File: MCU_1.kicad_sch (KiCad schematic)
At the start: 4 parts, among them U2 LPC55S28JBD100, Y1 24MHz

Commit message: Reset devresi eklenecek.
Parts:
- added C? (x2): 18pF, Resistor_SMD:R_0603_1608Metric, symbol Device:C
- added R?: R, symbol Device:R
- added SW?: SW_SPST, symbol Switch:SW_SPST
- added Y?: 24MHz, Crystal:Crystal_SMD_HC49-SD, symbol Device:Crystal
- U2: footprint erkan-hw-lib:HLQFP100 -> HLQFP100
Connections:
- net GND: now also C?.2, C?.2
- net MCU_XTAL32M_N: now also C?.1, Y?.1
- net MCU_XTAL32M_P: now also C?.1, Y?.2
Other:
- note added: "JTAG"
- note added: "MCU RESET"
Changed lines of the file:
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@@
   (junction (at 247.65 33.655) (diameter 0) (color 0 0 0 0)
   )
+  (junction (at 180.975 34.29) (diameter 0) (color 0 0 0 0)
+  )
   (junction (at 247.65 51.435) (diameter 0) (color 0 0 0 0)
   )
+  (junction (at 180.975 52.07) (diameter 0) (color 0 0 0 0)
+  )
   (wire (pts (xy 279.4 23.495) (xy 279.4 57.785))
     (stroke (width 0.5) (type solid) (color 57 87 255 1))
   )
+  (wire (pts (xy 191.135 34.29) (xy 180.975 34.29))
+    (stroke (width 0) (type default) (color 0 0 0 0))
+  )
   (wire (pts (xy 241.935 33.655) (xy 247.65 33.655))
     (stroke (width 0) (type default) (color 0 0 0 0))
@@
     (stroke (width 0) (type default) (color 0 0 0 0))
   )
+  (wire (pts (xy 223.52 100.965) (xy 280.035 100.965))
+    (stroke (width 0.5) (type solid) (color 57 87 255 1))
+  )
+  (wire (pts (xy 175.26 34.29) (xy 180.975 34.29))
+    (stroke (width 0) (type default) (color 0 0 0 0))
+  )
+  (wire (pts (xy 156.21 24.13) (xy 156.21 58.42))
+    (stroke (width 0.5) (type default) (color 57 87 255 1))
+  )
+  (wire (pts (xy 280.035 66.675) (xy 280.035 100.965))
+    (stroke (width 0.5) (type solid) (color 57 87 255 1))
+  )
   (wire (pts (xy 222.885 57.785) (xy 279.4 57.785))
     (stroke (width 0.5) (type solid) (color 57 87 255 1))
   )
+  (wire (pts (xy 191.135 52.07) (xy 180.975 52.07))
+    (stroke (width 0) (type default) (color 0 0 0 0))
+  )
+  (wire (pts (xy 223.52 66.675) (xy 280.035 66.675))
+    (stroke (width 0.5) (type default) (color 57 87 255 1))
+  )
   (wire (pts (xy 222.885 23.495) (xy 279.4 23.495))
     (stroke (width 0.5) (type default) (color 57 87 255 1))
   )
+  (wire (pts (xy 180.975 34.29) (xy 180.975 38.735))
+    (stroke (width 0) (type default) (color 0 0 0 0))
+  )
+  (wire (pts (xy 180.975 52.07) (xy 180.975 46.355))
+    (stroke (width 0) (type default) (color 0 0 0 0))
+  )
   (wire (pts (xy 247.65 33.655) (xy 247.65 38.1))
     (stroke (width 0) (type default) (color 0 0 0 0))
   )
+  (wire (pts (xy 175.26 52.07) (xy 180.975 52.07))
+    (stroke (width 0) (type default) (color 0 0 0 0))
+  )
+  (wire (pts (xy 223.52 66.675) (xy 223.52 100.965))
+    (stroke (width 0.5) (type default) (color 57 87 255 1))
+  )
+  (wire (pts (xy 156.21 24.13) (xy 212.725 24.13))
+    (stroke (width 0.5) (type default) (color 57 87 255 1))
+  )
+  (wire (pts (xy 212.725 24.13) (xy 212.725 58.42))
+    (stroke (width 0.5) (type solid) (color 57 87 255 1))
+  )
+  (wire (pts (xy 156.21 58.42) (xy 212.725 58.42))
+    (stroke (width 0.5) (type solid) (color 57 87 255 1))
+  )
   (wire (pts (xy 247.65 51.435) (xy 247.65 45.72))
     (stroke (width 0) (type default) (color 0 0 0 0))
@@
   (wire (pts (xy 257.81 33.655) (xy 247.65 33.655))
     (stroke (width 0) (type default) (color 0 0 0 0))
+  )
+  (text "JTAG" (at 155.575 23.495 0)
+    (effects (font (size 2.5 2.5) (thickness 0.5) bold) (justify left bottom))
   )
   (text "CRYSTAL-HSE" (at 222.25 22.86 0)
     (effects (font (size 2.5 2.5) (thickness 0.5) bold) (justify left bottom))
   )
+  (text "MCU RESET" (at 222.885 66.04 0)
+    (effects (font (size 2.5 2.5) (thickness 0.5) bold) (justify left bottom))
+  )
+  (label "MCU_XTAL32M_P" (at 175.26 34.29 180)
+    (effects (font (size 1.27 1.27)) (justify right bottom))
+  )
   (label "MCU_XTAL32M_P" (at 241.935 33.655 180)
     (effects (font (size 1.27 1.27)) (justify right bottom))
   )
-  (label "MCU_XTAL32M_P" (at 38.1 36.195 180)
-    (effects (font (size 1.27 1.27)) (justify right bottom))
-  )
-  (label "MCU_XTAL32M_N" (at 38.1 38.735 180)
+  (label "MCU_XTAL32M_P" (at 33.655 40.005 180)
+    (effects (font (size 1.27 1.27)) (justify right bottom))
+  )
+  (label "MCU_XTAL32M_N" (at 33.655 42.545 180)
     (effects (font (size 1.27 1.27)) (justify right bottom))
   )
   (label "MCU_XTAL32M_N" (at 241.935 51.435 180)
     (effects (font (size 1.27 1.27)) (justify right bottom))
+  )
+  (label "MCU_XTAL32M_N" (at 175.26 52.07 180)
+    (effects (font (size 1.27 1.27)) (justify right bottom))
+  )
+  (symbol (lib_id "Device:C") (at 194.945 52.07 90) (unit 1)
+    (in_bom yes) (on_board yes) (fields_autoplaced)
+    (property "Reference" "C?" (id 0) (at 194.945 45.085 90))
+    (property "Value" "18pF" (id 1) (at 194.945 47.625 90))
+    (property "Footprint" "Resistor_SMD:R_0603_1608Metric" (id 2) (at 198.755 51.1048 0)
+      (effects (font (size 1.27 1.27)) hide)
+    )
+    (property "Datasheet" "~" (id 3) (at 194.945 52.07 0)
+      (effects (font (size 1.27 1.27)) hide)
+    )
+    (pin "1")
+    (pin "2")
   )
   (symbol (lib_id "Device:C") (at 261.62 51.435 90) (unit 1)
@@
     (pin "1")
   )
-  (symbol (lib_id "erkan-hw:LPC55S28JBD100") (at 38.1 26.035 0) (unit 1)
-    (in_bom yes) (on_board yes) (fields_autoplaced)
-    (property "Reference" "U2" (id 0) (at 83.82 15.24 0)
+  (symbol (lib_id "Switch:SW_SPST") (at 243.84 84.455 0) (unit 1)
+    (in_bom yes) (on_board yes) (fields_autoplaced)
+    (property "Reference" "SW?" (id 0) (at 243.84 77.47 0))
+    (property "Value" "SW_SPST" (id 1) (at 243.84 80.01 0))
+    (property "Footprint" "" (id 2) (at 243.84 84.455 0)
+      (effects (font (size 1.27 1.27)) hide)
+    )
+    (property "Datasheet" "~" (id 3) (at 243.84 84.455 0)
+      (effects (font (size 1.27 1.27)) hide)
+    )
+    (pin "1")
+    (pin "2")
+  )
+  (symbol (lib_id "erkan-hw:LPC55S28JBD100") (at 17.145 29.845 0) (unit 1)
+    (in_bom yes) (on_board yes)
+    (property "Reference" "U2" (id 0) (at 79.375 18.415 0)
       (effects (font (size 1.524 1.524)))
     )
-    (property "Value" "LPC55S28JBD100" (id 1) (at 83.82 19.05 0)
+    (property "Value" "LPC55S28JBD100" (id 1) (at 79.375 22.225 0)
       (effects (font (size 1.524 1.524)))
     )
-    (property "Footprint" "erkan-hw-lib:HLQFP100" (id 2) (at 83.82 19.939 0)
+    (property "Footprint" "HLQFP100" (id 2) (at 37.465 14.859 0)
       (effects (font (size 1.524 1.524)) hide)
     )
-    (property "Datasheet" "" (id 3) (at 38.1 26.035 0)
+    (property "Datasheet" "" (id 3) (at 17.145 29.845 0)
       (effects (font (size 1.524 1.524)))
     )
@@
     (pin "42")
     (pin "43")
-    (pin "45")
-    (pin "48")
-    (pin "49")
     (pin "5")
-    (pin "50")
-    (pin "51")
     (pin "52")
     (pin "53")
@@
     (pin "33")
     (pin "37")
-    (pin "39")
     (pin "44")
-    (pin "46")
-    (pin "47")
     (pin "63")
     (pin "69")
@@
     (pin "95")
     (pin "99")
+    (pin "39")
+    (pin "45")
+    (pin "46")
+    (pin "47")
+    (pin "48")
+    (pin "49")
+    (pin "50")
+    (pin "51")
   )
   (symbol (lib_id "power:GND") (at 265.43 33.655 90) (unit 1)
@@
     (pin "2")
   )
+  (symbol (lib_id "power:GND") (at 198.755 34.29 90) (unit 1)
+    (in_bom yes) (on_board yes) (fields_autoplaced)
+    (property "Reference" "#PWR?" (id 0) (at 205.105 34.29 0)
+      (effects (font (size 1.27 1.27)) hide)
+    )
+    (property "Value" "GND" (id 1) (at 202.565 34.2899 90)
+      (effects (font (size 1.27 1.27)) (justify right))
+    )
+    (property "Footprint" "" (id 2) (at 198.755 34.29 0)
+      (effects (font (size 1.27 1.27)) hide)
+    )
+    (property "Datasheet" "" (id 3) (at 198.755 34.29 0)
+      (effects (font (size 1.27 1.27)) hide)
+    )
+    (pin "1")
+  )
+  (symbol (lib_id "Device:Crystal") (at 180.975 42.545 90) (unit 1)
+    (in_bom yes) (on_board yes) (fields_autoplaced)
+    (property "Reference" "Y?" (id 0) (at 184.785 41.2749 90)
+      (effects (font (size 1.27 1.27)) (justify right))
+    )
+    (property "Value" "24MHz" (id 1) (at 184.785 43.8149 90)
+      (effects (font (size 1.27 1.27)) (justify right))
+    )
+    (property "Footprint" "Crystal:Crystal_SMD_HC49-SD" (id 2) (at 180.975 42.545 0)
+      (effects (font (size 1.27 1.27)) hide)
+    )
+    (property "Datasheet" "~" (id 3) (at 180.975 42.545 0)
+      (effects (font (size 1.27 1.27)) hide)
+    )
+    (pin "1")
+    (pin "2")
+  )
+  (symbol (lib_id "Device:C") (at 194.945 34.29 90) (unit 1)
+    (in_bom yes) (on_board yes) (fields_autoplaced)
+    (property "Reference" "C?" (id 0) (at 194.945 27.305 90))
+    (property "Value" "18pF" (id 1) (at 194.945 29.845 90))
+    (property "Footprint" "Resistor_SMD:R_0603_1608Metric" (id 2) (at 198.755 33.3248 0)
+      (effects (font (size 1.27 1.27)) hide)
+    )
+    (property "Datasheet" "~" (id 3) (at 194.945 34.29 0)
+      (effects (font (size 1.27 1.27)) hide)
+    )
+    (pin "1")
+    (pin "2")
+  )
   (symbol (lib_id "Device:Crystal") (at 247.65 41.91 90) (unit 1)
     (in_bom yes) (on_board yes) (fields_autoplaced)
@@
       (effects (font (size 1.27 1.27)) hide)
     )
+    (pin "1")
+    (pin "2")
+  )
+  (symbol (lib_id "power:GND") (at 198.755 52.07 90) (unit 1)
+    (in_bom yes) (on_board yes) (fields_autoplaced)
+    (property "Reference" "#PWR?" (id 0) (at 205.105 52.07 0)
+      (effects (font (size 1.27 1.27)) hide)
+    )
+    (property "Value" "GND" (id 1) (at 202.565 52.0699 90)
+      (effects (font (size 1.27 1.27)) (justify right))
+    )
+    (property "Footprint" "" (id 2) (at 198.755 52.07 0)
+      (effects (font (size 1.27 1.27)) hide)
+    )
+    (property "Datasheet" "" (id 3) (at 198.755 52.07 0)
+      (effects (font (size 1.27 1.27)) hide)
+    )
+    (pin "1")
+  )
+  (symbol (lib_id "Device:R") (at 252.095 76.835 180) (unit 1)
+    (in_bom yes) (on_board yes) (fields_autoplaced)
+    (property "Reference" "R?" (id 0) (at 254 75.5649 0)
+      (effects (font (size 1.27 1.27)) (justify right))
+    )
+    (property "Value" "R" (id 1) (at 254 78.1049 0)
+      (effects (font (size 1.27 1.27)) (justify right))
+    )
+    (property "Footprint" "" (id 2) (at 253.873 76.835 90)
+      (effects (font (size 1.27 1.27)) hide)
+    )
+    (property "Datasheet" "~" (id 3) (at 252.095 76.835 0)
+      (effects (font (size 1.27 1.27)) hide)
+    )

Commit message: JTAG bağlantıları tamamlanacak
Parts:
- removed C? (x2): 18pF, Resistor_SMD:R_0603_1608Metric, symbol Device:C
- removed Y?: 24MHz, Crystal:Crystal_SMD_HC49-SD, symbol Device:Crystal
- added C?: C_Small, symbol Device:C_Small
- added J?: JLink, Connector_IDC:IDC-Header_2x05_P2.54mm_Vertical, symbol Connector_Generic:Conn_02x05_Odd_Even
- added J?: JLink, Connector_PinHeader_1.27mm:PinHeader_2x05_P1.27mm_Vertical, symbol Connector_Generic:Conn_02x05_Odd_Even
- added R? (x3): 100k, symbol Device:R_Small_US
- added R?: 10k, symbol Device:R_Small_US
- added R?: 0, symbol Device:R_Small_US
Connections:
- net GND: now also J?.3 (Pin_3), J?.3 (Pin_3), J?.5 (Pin_5), J?.5 (Pin_5), R?.1
- net MCU_XTAL32M_N: now also U2.28 (XTAL32M_N); no longer U2.52 (XTAL32K_P)
- net at SW?.2 (B): now also R?.1
- net LPC_RESET: now reaches U2.32 (RESETN)
- net LPC_RESET: now also J?.10 (Pin_10), R?.1
- net MCU_XTAL32K_N: now reaches U2.53 (XTAL32K_N)
- net TRST: now reaches U2.81 (PIO0_2/TRST)
- net TCK/SWCLK: now reaches U2.83 (PIO0_3/TCK)
- net TCK/SWCLK: now also J?.4 (Pin_4)
- net TMS/SWDIO: now reaches U2.86 (PIO0_4/TMS)
- net TMS/SWDIO: now also J?.2 (Pin_2), J?.2 (Pin_2), R?.1
- net TDI: now reaches U2.88 (PIO0_5/TDI)
- net TDI: now also J?.8 (Pin_8)
- net TDO/SWO: now reaches U2.89 (PIO0_6/TDO)
- net TDO/SWO: now also J?.6 (Pin_6), J?.6 (Pin_6)
- new net: J?.1 (Pin_1), R?.2
- new net: J?.4 (Pin_4), R?.1, R?.2
- new net MCU_XTAL32K_P: U2.52 (XTAL32K_P)
- new net TDI/N.C.: J?.8 (Pin_8)
- new net V_TARGET: J?.1 (Pin_1), R?.1, R?.2, R?.2, R?.2
- new net nRESET: J?.10 (Pin_10)
- no-connect marks 0 -> 4

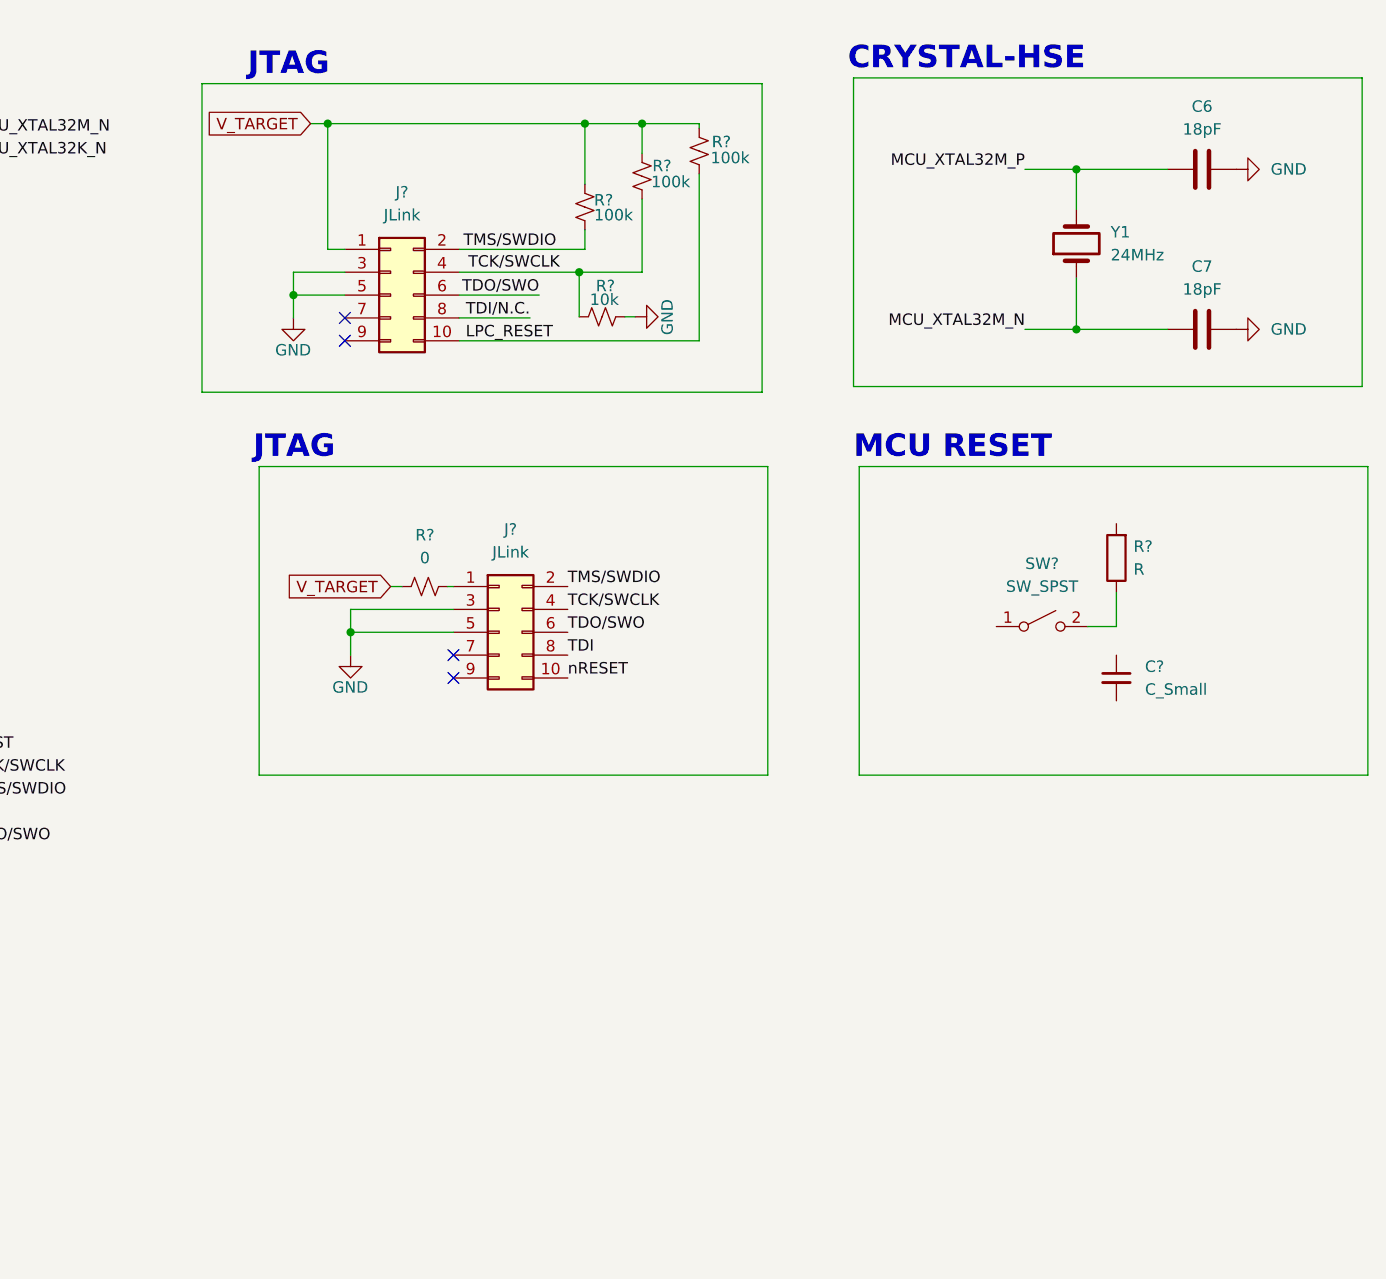
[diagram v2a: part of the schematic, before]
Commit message: ISP Boot eklenecek
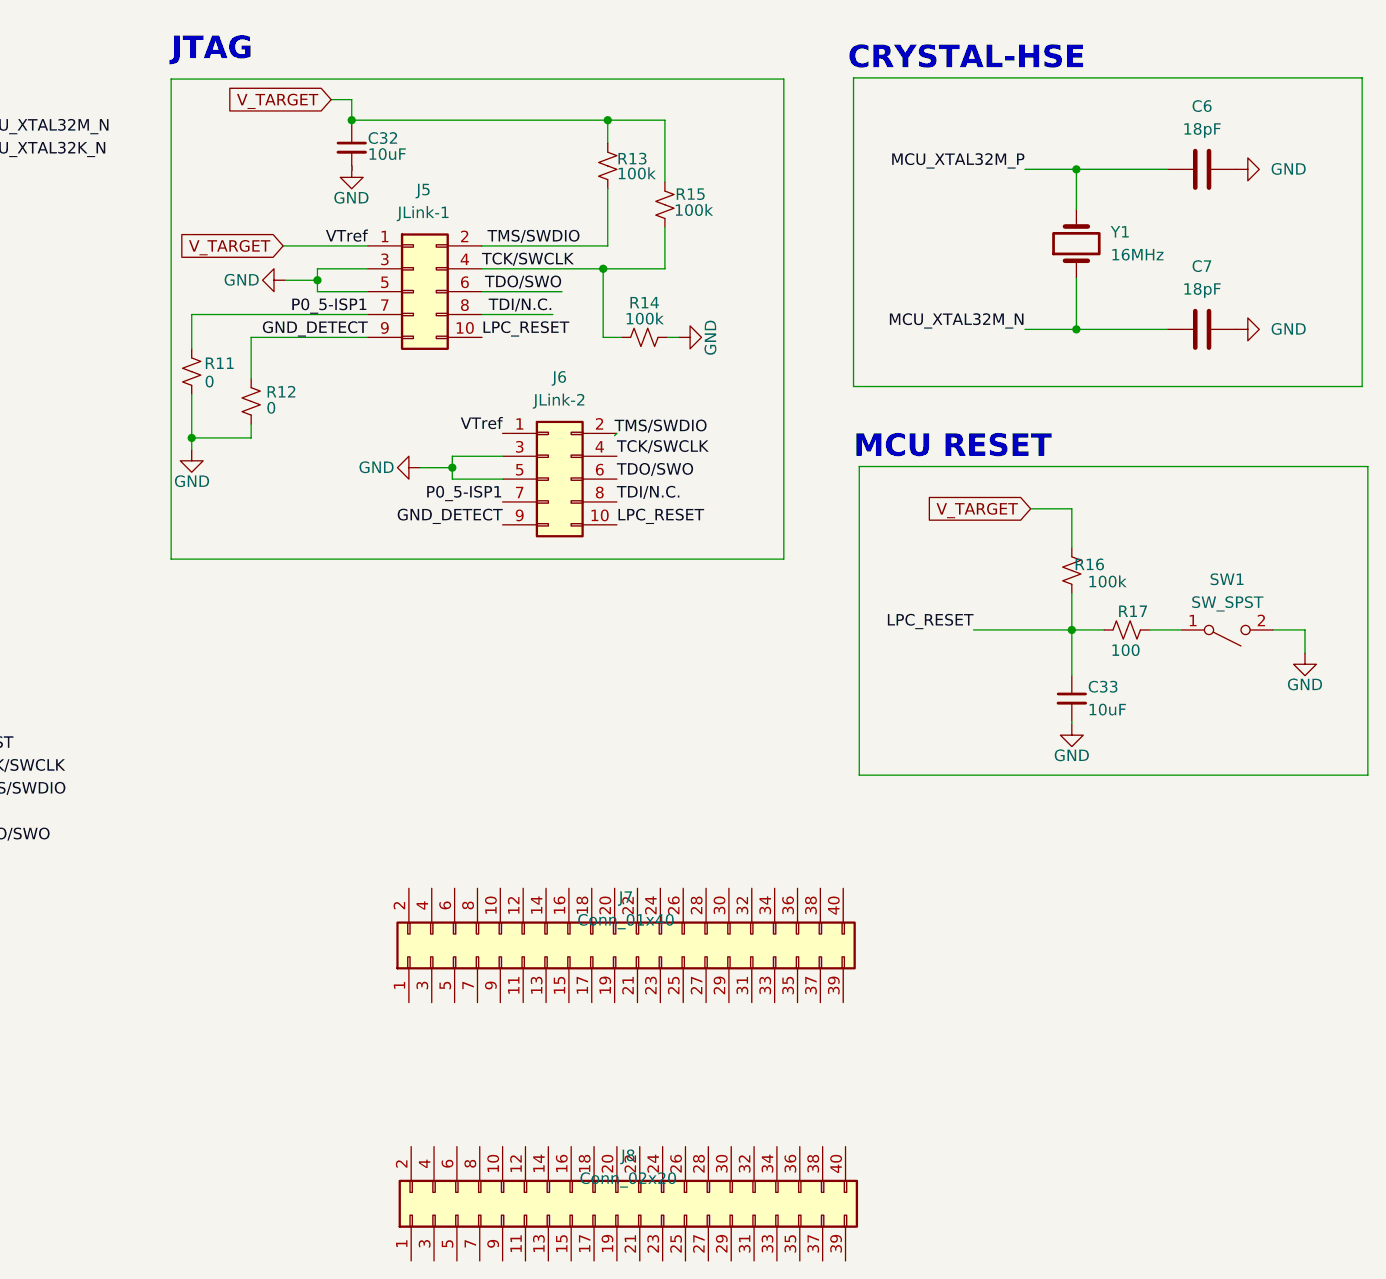
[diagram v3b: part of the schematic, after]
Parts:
- removed R?: 100k, symbol Device:R_Small_US
- removed R?: 10k, symbol Device:R_Small_US
- removed R?: R, symbol Device:R
- removed R?: 0, symbol Device:R_Small_US
- added C32: 10uF, Capacitor_SMD:C_0603_1608Metric, symbol Device:C_Small
- added J7: Conn_01x40, Connector_PinSocket_2.54mm:PinSocket_1x40_P2.54mm_Vertical, symbol Connector_Generic:Conn_02x20_Odd_Even
- added J8: Conn_02x20, Connector_PinSocket_2.54mm:PinSocket_2x20_P2.54mm_Vertical, symbol Connector_Generic:Conn_02x20_Odd_Even
- added R11, R12: 0, Resistor_SMD:R_0603_1608Metric, symbol Device:R_Small_US
- added R14, R16: 100k, Resistor_SMD:R_0603_1608Metric, symbol Device:R_Small_US
- added R17: 100, Resistor_SMD:R_0603_1608Metric, symbol Device:R_Small_US
- C33: renamed from C?; value C_Small -> 10uF; footprint (none) -> Capacitor_SMD:C_0603_1608Metric
- C6, C7: footprint Resistor_SMD:R_0603_1608Metric -> Capacitor_SMD:C_0603_1608Metric
- J5: renamed from J?; value JLink -> JLink-1
- J6: renamed from J?; value JLink -> JLink-2
- R13, R15: renamed from R?; footprint (none) -> Resistor_SMD:R_0603_1608Metric
- SW1: renamed from SW?; footprint (none) -> Button_Switch_SMD:SW_SPST_CK_RS282G05A3
- U2: footprint HLQFP100 -> erkan-hw-lib:HLQFP100
- Y1: value 24MHz -> 16MHz
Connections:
- net nRESET is gone; now on net LPC_RESET: J6.10 (Pin_10)
- net GND: now also C33.2, SW1.2 (B), C32.2, R11.2, R12.2, R14.1
- net LPC_RESET: now also C33.1, R16.2, R17.1
- net TCK/SWCLK: now also J5.4 (Pin_4), R15.1, R14.2
- net TDI: no longer J6.8 (Pin_8)
- net TDI/N.C.: now also J6.8 (Pin_8)
- net V_TARGET: now also J6.1 (Pin_1), C32.1, R16.1
- net P0_5-ISP1: now reaches J6.7 (Pin_7)
- net P0_5-ISP1: now also J5.7 (Pin_7), R11.1
- net GND_DETECT: now reaches J6.9 (Pin_9)
- net GND_DETECT: now also J5.9 (Pin_9), R12.1
- net at SW1.1 (A): now also R17.2
- no-connect marks 4 -> 0
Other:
- moved on the sheet: C33, J5, J6, R13, R15, SW1

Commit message: Schematic updated
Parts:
- added R18: 100k, Resistor_SMD:R_0603_1608Metric, symbol Device:R_Small_US
- added R19: 100, Resistor_SMD:R_0603_1608Metric, symbol Device:R_Small_US
- added SW2: SW_SPST, Button_Switch_SMD:SW_SPST_PTS645, symbol Switch:SW_SPST
- J7: value Conn_01x40 -> Conn_02x20; footprint Connector_PinSocket_2.54mm:PinSocket_1x40_P2.54mm_Vertical -> Connector_PinSocket_2.54mm:PinSocket_2x20_P2.54mm_Vertical
- SW1: footprint Button_Switch_SMD:SW_SPST_CK_RS282G05A3 -> Button_Switch_SMD:SW_SPST_PTS645
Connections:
- net GND: now also SW2.2 (B)
- net P0_5-ISP1: now also R18.2, R19.2
- net V_TARGET: now also R18.1
- new net: R19.1, SW2.1 (A)
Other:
- note added: "BUTTONS"
- moved on the sheet: J7, J8
